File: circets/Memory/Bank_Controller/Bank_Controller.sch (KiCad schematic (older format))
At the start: 22 parts

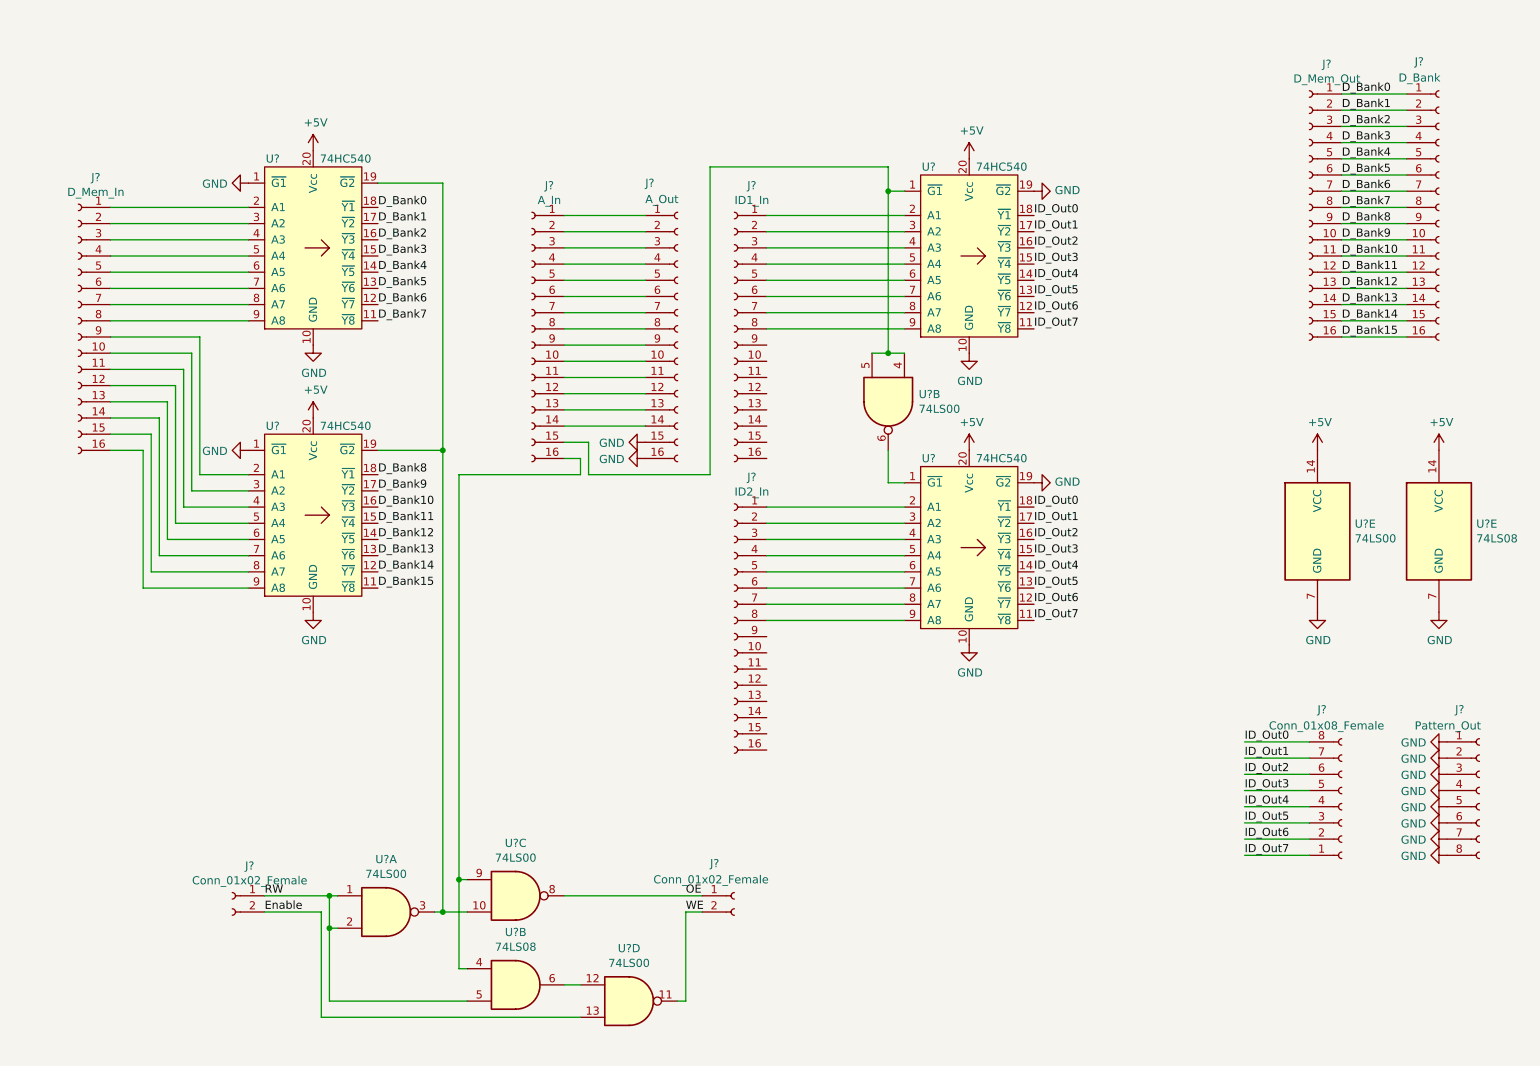
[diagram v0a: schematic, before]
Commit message: Fixed alot of Issues in Memory Module
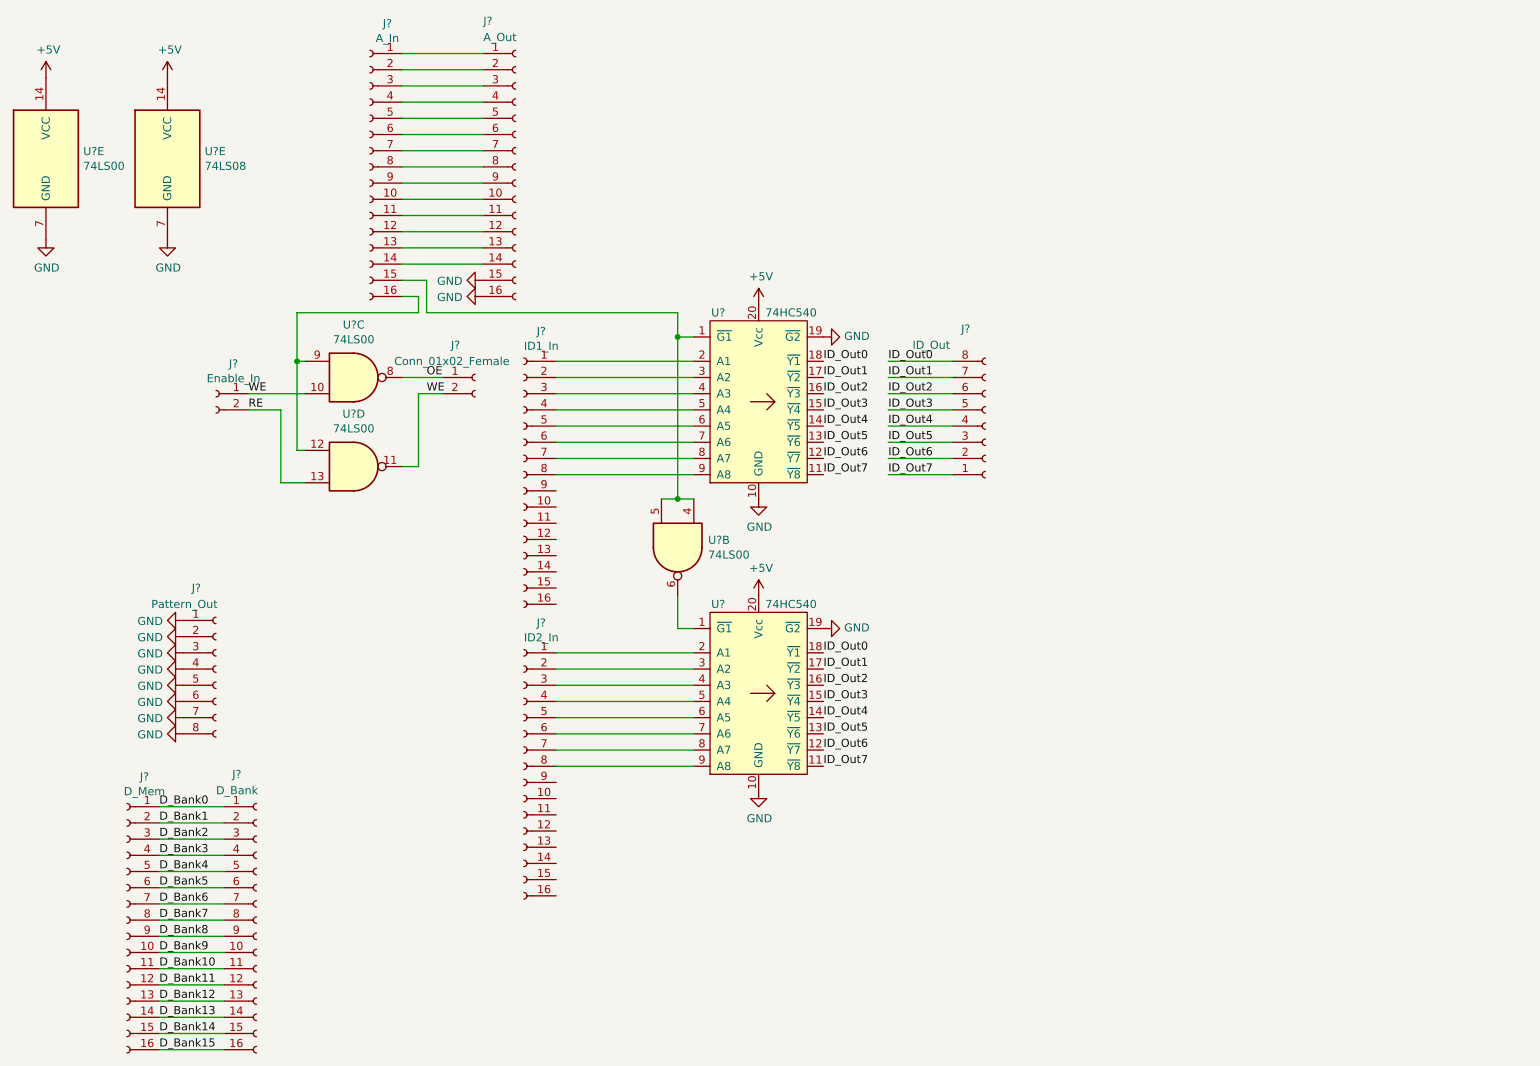
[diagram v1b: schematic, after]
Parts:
- removed J?: D_Mem_In, symbol Connector:Conn_01x16_Female
- removed U? (x2): 74HC540, symbol Computer_Component_Library:74HC540
- removed U?: 74LS00, symbol 74xx:74LS00
- removed U?: 74LS08, symbol 74xx:74LS08
- J?: value D_Mem_Out -> D_Mem
- J?: value Conn_01x08_Female -> ID_Out
- J?: value Conn_01x02_Female -> Enable_In
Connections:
- net RW is gone; now on net WE: J?.1 (Pin_1)
- net WE: now also U?.10
- net at J?.16 (Pin_16), U?.9: now also U?.12
- net Enable renamed RE
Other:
- moved on the sheet: J?, U?, U?B, U?C, U?D, U?E
